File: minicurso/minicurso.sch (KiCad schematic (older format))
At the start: 4 parts

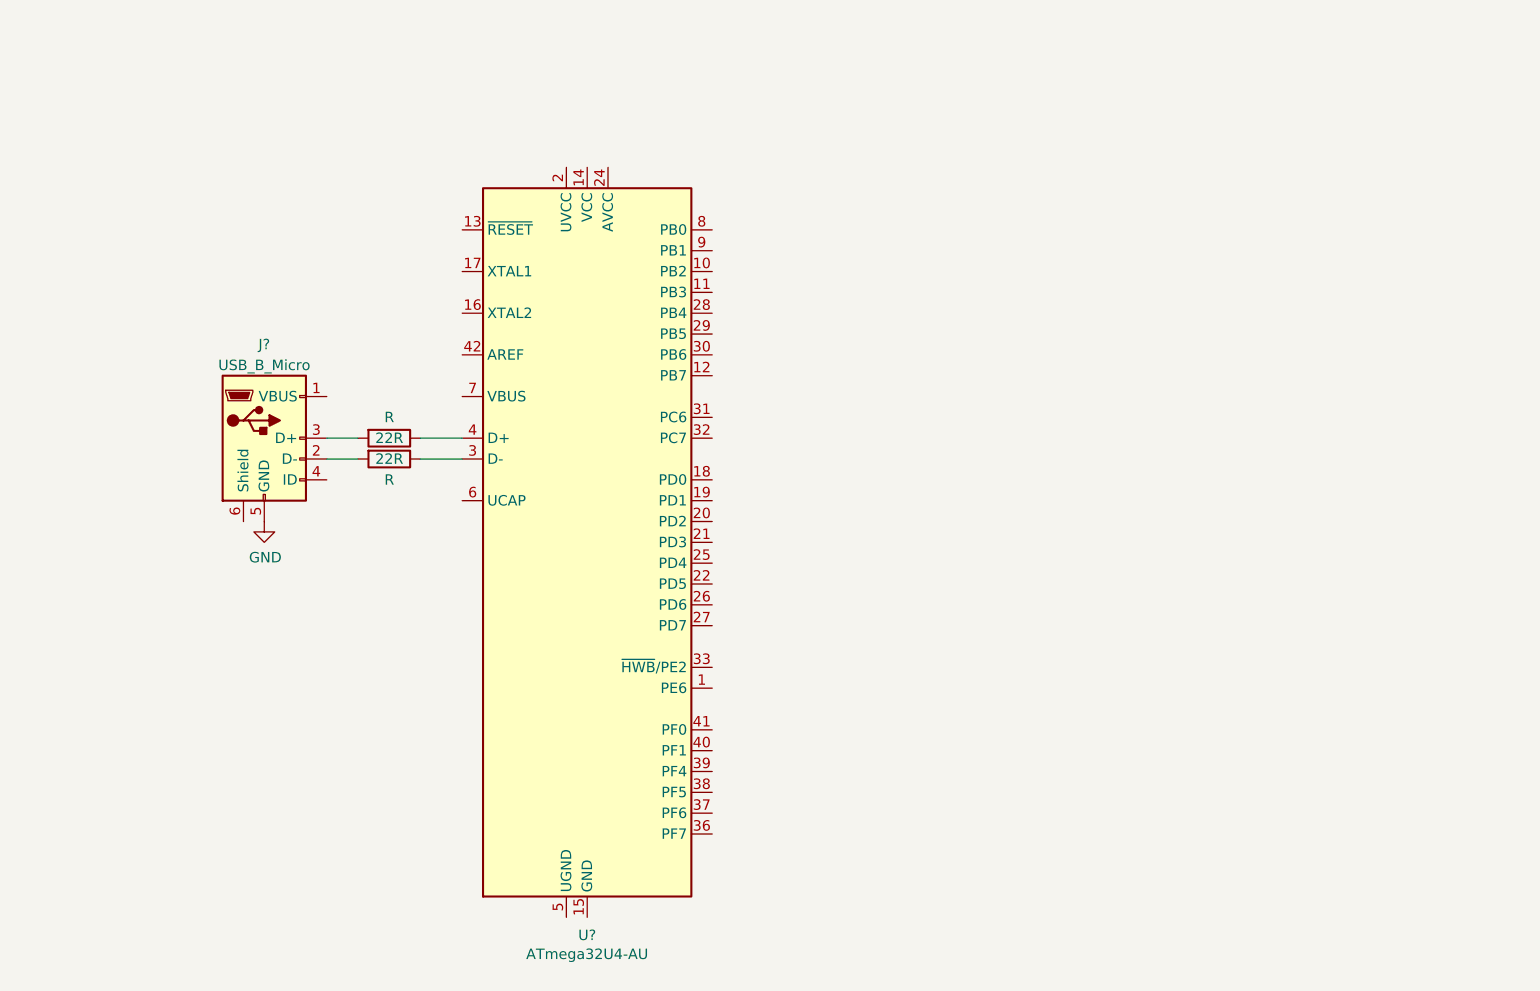
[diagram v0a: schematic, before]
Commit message: Add crystal, ucamp and bypass
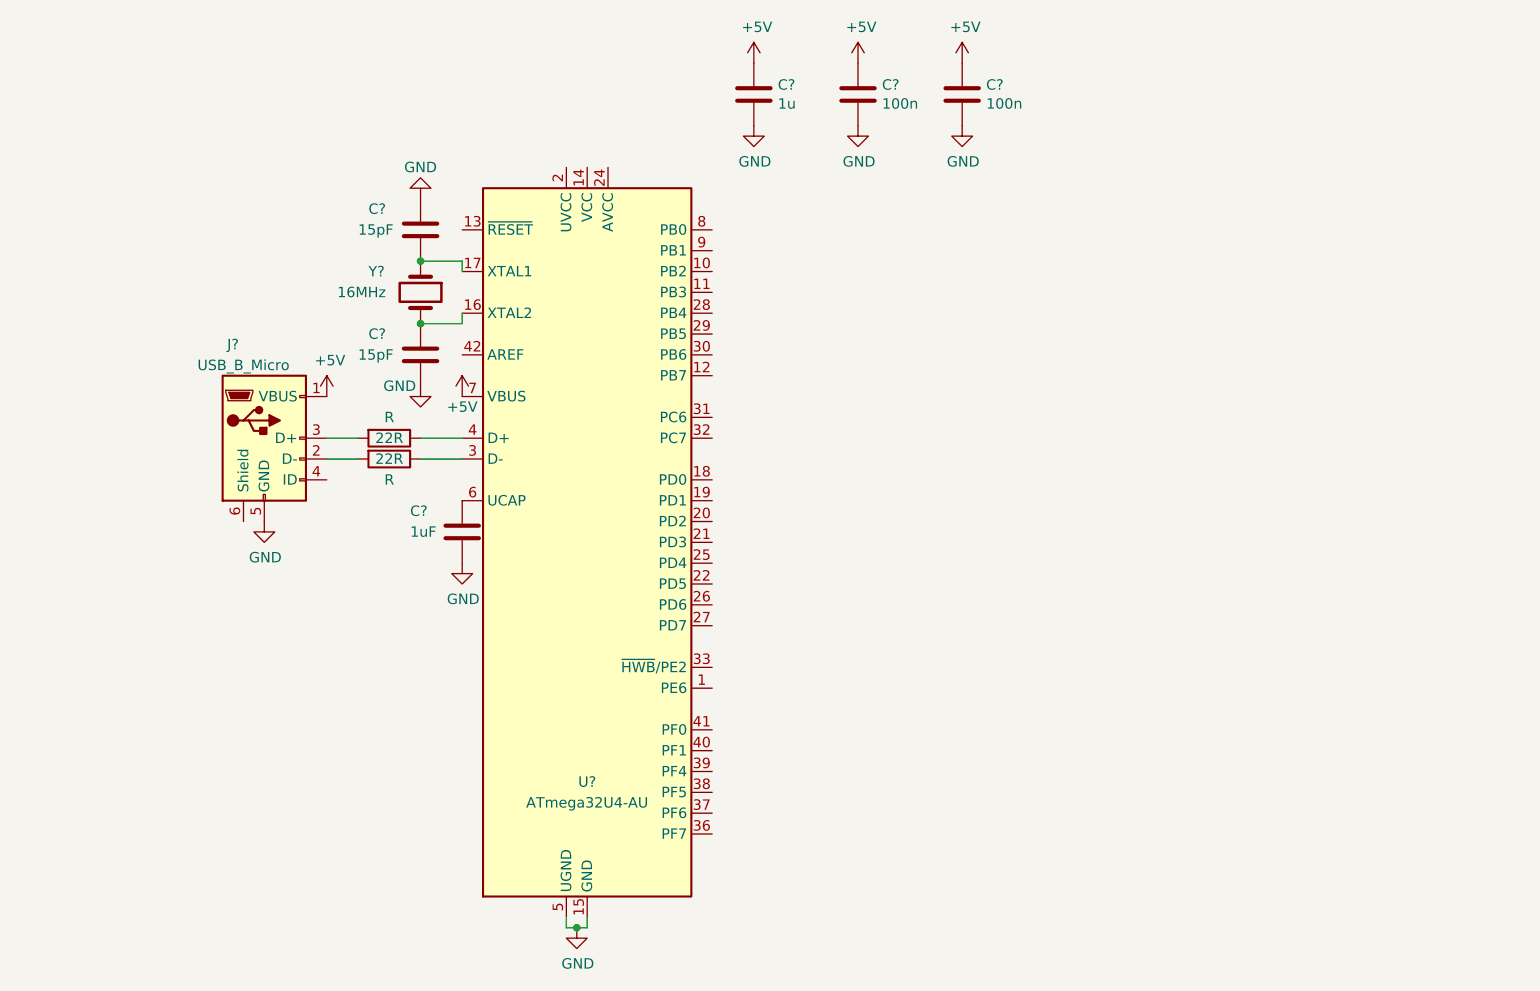
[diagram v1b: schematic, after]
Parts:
- added C? (x2): 15pF, symbol Device:C
- added C?: 1uF, symbol Device:C
- added C?: 1u, symbol Device:C
- added C? (x2): 100n, symbol Device:C
- added Y?: 16MHz, symbol Device:Crystal
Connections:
- net GND: now also U?.15 (GND), U?.23 (GND), U?.35 (GND), U?.43 (GND), U?.5 (UGND), C?.1, C?.2, C?.2, C?.2, C?.2, C?.2
- net at U?.16 (XTAL2): now also C?.1, Y?.2
- net at U?.17 (XTAL1): now also C?.2, Y?.1
- net at U?.6 (UCAP): now also C?.1
- net +5V: now reaches U?.7 (VBUS)
- net +5V: now also J?.1 (VBUS), C?.1, C?.1, C?.1
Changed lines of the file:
@@
 U 1 1 5D7A3DE3
 P 4000 3000
-F 0 "U?" H 4000 1114 50  0000 C CNN
-F 1 "ATmega32U4-AU" H 4000 1023 50  0000 C CNN
+F 0 "U?" H 4000 1850 50  0000 C CNN
+F 1 "ATmega32U4-AU" H 4000 1750 50  0000 C CNN
 F 2 "Package_QFP:TQFP-44_10x10mm_P0.8mm" H 4000 3000 50  0001 C CIN
 F 3 "http://ww1.microchip.com/downloads/en/DeviceDoc/Atmel-7766-8-bit-AVR-ATmega16U4-32U4_Datasheet.pdf" H 4000 3000 50  0001 C CNN
@@
 U 1 1 5D7A3F22
 P 2450 2500
-F 0 "J?" H 2450 2950 50  0000 C CNN
-F 1 "USB_B_Micro" H 2450 2850 50  0000 C CNN
+F 0 "J?" H 2300 2950 50  0000 C CNN
+F 1 "USB_B_Micro" H 2350 2850 50  0000 C CNN
 F 2 "" H 2600 2450 50  0001 C CNN
 F 3 "~" H 2600 2450 50  0001 C CNN
@@
 	1    0    0    -1
 $EndComp
+$Comp
+L power:GND #PWR?
+U 1 1 5D7A4F01
+P 3950 4850
+F 0 "#PWR?" H 3950 4600 50  0001 C CNN
+F 1 "GND" H 3955 4677 50  0000 C CNN
+F 2 "" H 3950 4850 50  0001 C CNN
+F 3 "" H 3950 4850 50  0001 C CNN
+	1    3950 4850
+	1    0    0    -1
+$EndComp
+Wire Wire Line
+	4000 4850 3950 4850
+Wire Wire Line
+	3900 4850 3900 4800
+Connection ~ 3950 4850
+Wire Wire Line
+	3950 4850 3900 4850
+Wire Wire Line
+	4000 4850 4000 4800
+$Comp
+L Device:Crystal Y?
+U 1 1 5D7A53EA
+P 3200 1800
+F 0 "Y?" V 3100 1550 50  0000 L CNN
+F 1 "16MHz" V 3200 1400 50  0000 L CNN
+F 2 "" H 3200 1800 50  0001 C CNN
+F 3 "~" H 3200 1800 50  0001 C CNN
+	1    3200 1800
+	0    1    1    0
+$EndComp
+Wire Wire Line
+	3400 1650 3400 1700
+Wire Wire Line
+	3400 1950 3400 1900
+Wire Wire Line
+	3200 1950 3400 1950
+Wire Wire Line
+	3200 1650 3400 1650
+$Comp
+L Device:C C?
+U 1 1 5D7A6541
+P 3200 1500
+F 0 "C?" H 2950 1600 50  0000 L CNN
+F 1 "15pF" H 2900 1500 50  0000 L CNN
+F 2 "" H 3238 1350 50  0001 C CNN
+F 3 "~" H 3200 1500 50  0001 C CNN
+	1    3200 1500
+	1    0    0    -1
+$EndComp
+Connection ~ 3200 1650
+$Comp
+L power:GND #PWR?
+U 1 1 5D7A65E6
+P 3200 1350
+F 0 "#PWR?" H 3200 1100 50  0001 C CNN
+F 1 "GND" H 3200 1200 50  0000 C CNN
+F 2 "" H 3200 1350 50  0001 C CNN
+F 3 "" H 3200 1350 50  0001 C CNN
+	1    3200 1350
+	-1   0    0    1
+$EndComp
+$Comp
+L Device:C C?
+U 1 1 5D7A66D4
+P 3200 2100
+F 0 "C?" H 2950 2200 50  0000 L CNN
+F 1 "15pF" H 2900 2100 50  0000 L CNN
+F 2 "" H 3238 1950 50  0001 C CNN
+F 3 "~" H 3200 2100 50  0001 C CNN
+	1    3200 2100
+	1    0    0    -1
+$EndComp
+Connection ~ 3200 1950
+$Comp
+L power:GND #PWR?
+U 1 1 5D7A6801
+P 3200 2250
+F 0 "#PWR?" H 3200 2000 50  0001 C CNN
+F 1 "GND" H 3100 2250 50  0000 C CNN
+F 2 "" H 3200 2250 50  0001 C CNN
+F 3 "" H 3200 2250 50  0001 C CNN
+	1    3200 2250
+	1    0    0    -1
+$EndComp
+$Comp
+L power:+5V #PWR?
+U 1 1 5D7A6D12
+P 2750 2300
+F 0 "#PWR?" H 2750 2150 50  0001 C CNN
+F 1 "+5V" H 2765 2473 50  0000 C CNN
+F 2 "" H 2750 2300 50  0001 C CNN
+F 3 "" H 2750 2300 50  0001 C CNN
+	1    2750 2300
+	1    0    0    -1
+$EndComp
+$Comp
+L power:+5V #PWR?
+U 1 1 5D7A6EC6
+P 3400 2300
+F 0 "#PWR?" H 3400 2150 50  0001 C CNN
+F 1 "+5V" H 3400 2250 50  0000 C CNN
+F 2 "" H 3400 2300 50  0001 C CNN
+F 3 "" H 3400 2300 50  0001 C CNN
+	1    3400 2300
+	1    0    0    -1
+$EndComp
+$Comp
+L Device:C C?
+U 1 1 5D7A6F9F
+P 3400 2950
+F 0 "C?" H 3150 3050 50  0000 L CNN
+F 1 "1uF" H 3150 2950 50  0000 L CNN
+F 2 "" H 3438 2800 50  0001 C CNN
+F 3 "~" H 3400 2950 50  0001 C CNN
+	1    3400 2950
+	1    0    0    -1
+$EndComp
+$Comp
+L power:GND #PWR?
+U 1 1 5D7A6FFB
+P 3400 3100
+F 0 "#PWR?" H 3400 2850 50  0001 C CNN
+F 1 "GND" H 3405 2927 50  0000 C CNN
+F 2 "" H 3400 3100 50  0001 C CNN
+F 3 "" H 3400 3100 50  0001 C CNN
+	1    3400 3100
+	1    0    0    -1
+$EndComp
+$Comp
+L power:+5V #PWR?
+U 1 1 5D7A4BAC
+P 4800 700
+F 0 "#PWR?" H 4800 550 50  0001 C CNN
+F 1 "+5V" H 4815 873 50  0000 C CNN
+F 2 "" H 4800 700 50  0001 C CNN
+F 3 "" H 4800 700 50  0001 C CNN
+	1    4800 700
+	1    0    0    -1
+$EndComp
+$Comp
+L Device:C C?
+U 1 1 5D7A7E2D
+P 4800 850
+F 0 "C?" H 4915 896 50  0000 L CNN
+F 1 "1u" H 4915 805 50  0000 L CNN
+F 2 "" H 4838 700 50  0001 C CNN
+F 3 "~" H 4800 850 50  0001 C CNN
+	1    4800 850
+	1    0    0    -1
+$EndComp
+$Comp
+L power:GND #PWR?
+U 1 1 5D7A7F18
+P 4800 1000
+F 0 "#PWR?" H 4800 750 50  0001 C CNN
+F 1 "GND" H 4805 827 50  0000 C CNN
+F 2 "" H 4800 1000 50  0001 C CNN
+F 3 "" H 4800 1000 50  0001 C CNN
+	1    4800 1000
+	1    0    0    -1
+$EndComp
+$Comp
+L Device:C C?
+U 1 1 5D7A81A9
+P 5300 850
+F 0 "C?" H 5415 896 50  0000 L CNN
+F 1 "100n" H 5415 805 50  0000 L CNN
+F 2 "" H 5338 700 50  0001 C CNN
+F 3 "~" H 5300 850 50  0001 C CNN
+	1    5300 850
+	1    0    0    -1
+$EndComp
+$Comp
+L power:+5V #PWR?
+U 1 1 5D7A8211
+P 5300 700
+F 0 "#PWR?" H 5300 550 50  0001 C CNN
+F 1 "+5V" H 5315 873 50  0000 C CNN
+F 2 "" H 5300 700 50  0001 C CNN
+F 3 "" H 5300 700 50  0001 C CNN
+	1    5300 700
+	1    0    0    -1
+$EndComp
+$Comp
+L power:GND #PWR?
+U 1 1 5D7A8230
+P 5300 1000
+F 0 "#PWR?" H 5300 750 50  0001 C CNN
+F 1 "GND" H 5305 827 50  0000 C CNN
+F 2 "" H 5300 1000 50  0001 C CNN
+F 3 "" H 5300 1000 50  0001 C CNN
+	1    5300 1000
+	1    0    0    -1
+$EndComp
+$Comp
+L Device:C C?
+U 1 1 5D7A841B
+P 5800 850
+F 0 "C?" H 5915 896 50  0000 L CNN
+F 1 "100n" H 5915 805 50  0000 L CNN
+F 2 "" H 5838 700 50  0001 C CNN
+F 3 "~" H 5800 850 50  0001 C CNN
+	1    5800 850
+	1    0    0    -1
+$EndComp
+$Comp
+L power:+5V #PWR?
+U 1 1 5D7A8457
+P 5800 700
+F 0 "#PWR?" H 5800 550 50  0001 C CNN
+F 1 "+5V" H 5815 873 50  0000 C CNN
+F 2 "" H 5800 700 50  0001 C CNN
+F 3 "" H 5800 700 50  0001 C CNN
+	1    5800 700
+	1    0    0    -1
+$EndComp
+$Comp
+L power:GND #PWR?
+U 1 1 5D7A8478
+P 5800 1000
+F 0 "#PWR?" H 5800 750 50  0001 C CNN
+F 1 "GND" H 5805 827 50  0000 C CNN
+F 2 "" H 5800 1000 50  0001 C CNN
+F 3 "" H 5800 1000 50  0001 C CNN
+	1    5800 1000
+	1    0    0    -1
+$EndComp

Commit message: Add reset and pinheaders
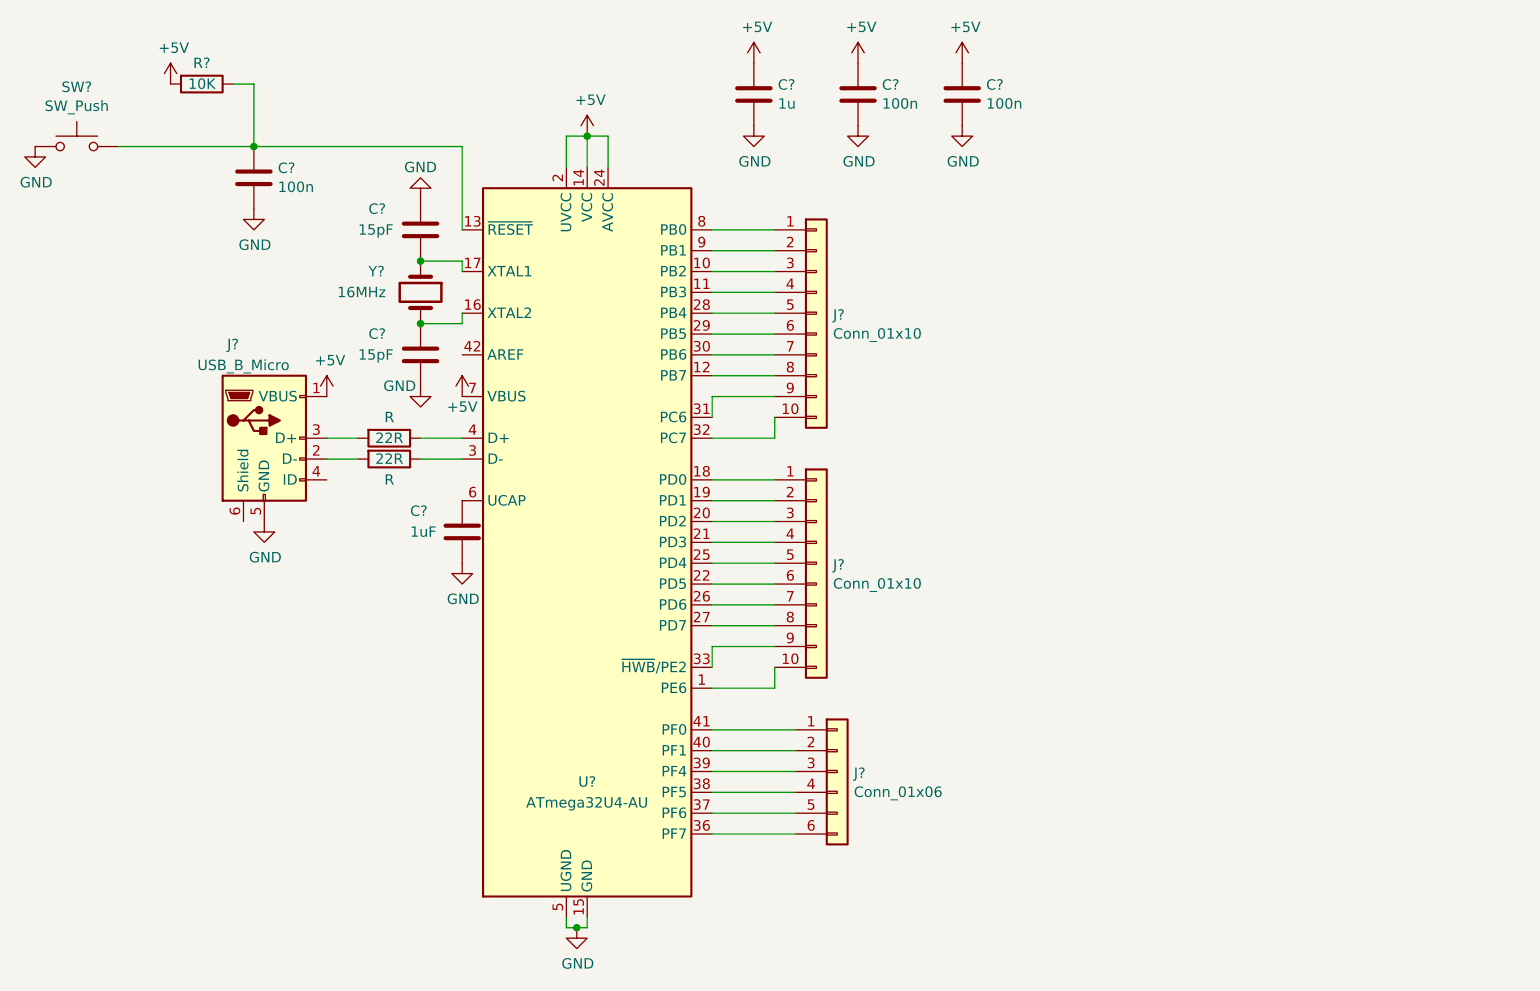
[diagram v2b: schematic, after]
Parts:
- added C?: 100n, symbol Device:C
- added J? (x2): Conn_01x10, symbol Connector_Generic:Conn_01x10
- added J?: Conn_01x06, symbol Connector_Generic:Conn_01x06
- added R?: 10K, symbol Device:R
- added SW?: SW_Push, symbol Switch:SW_Push
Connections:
- net +5V: now also U?.14 (VCC), U?.2 (UVCC), U?.24 (AVCC), U?.34 (VCC), U?.44 (AVCC), R?.2
- net GND: now also C?.2, SW?.1
- net at U?.1 (PE6): now also J?.10 (Pin_10)
- net at U?.10 (PB2): now also J?.3 (Pin_3)
- net at U?.11 (PB3): now also J?.4 (Pin_4)
- net at U?.12 (PB7): now also J?.8 (Pin_8)
- net at U?.13 (~RESET): now also C?.1, R?.1, SW?.2
- net at U?.18 (PD0): now also J?.1 (Pin_1)
- net at U?.19 (PD1): now also J?.2 (Pin_2)
- net at U?.20 (PD2): now also J?.3 (Pin_3)
- net at U?.21 (PD3): now also J?.4 (Pin_4)
- net at U?.22 (PD5): now also J?.6 (Pin_6)
- net at U?.25 (PD4): now also J?.5 (Pin_5)
- net at U?.26 (PD6): now also J?.7 (Pin_7)
- net at U?.27 (PD7): now also J?.8 (Pin_8)
- net at U?.28 (PB4): now also J?.5 (Pin_5)
- net at U?.29 (PB5): now also J?.6 (Pin_6)
- net at U?.30 (PB6): now also J?.7 (Pin_7)
- net at U?.31 (PC6): now also J?.9 (Pin_9)
- net at U?.32 (PC7): now also J?.10 (Pin_10)
- net at U?.33 (~HWB~/PE2): now also J?.9 (Pin_9)
- net at U?.36 (PF7): now also J?.6 (Pin_6)
- net at U?.37 (PF6): now also J?.5 (Pin_5)
- net at U?.38 (PF5): now also J?.4 (Pin_4)
- net at U?.39 (PF4): now also J?.3 (Pin_3)
- net at U?.40 (PF1): now also J?.2 (Pin_2)
- net at U?.41 (PF0): now also J?.1 (Pin_1)
- net at U?.8 (PB0): now also J?.1 (Pin_1)
- net at U?.9 (PB1): now also J?.2 (Pin_2)
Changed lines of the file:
@@
 	1    0    0    -1
 $EndComp
+$Comp
+L power:+5V #PWR?
+U 1 1 5D7A8686
+P 4000 1050
+F 0 "#PWR?" H 4000 900 50  0001 C CNN
+F 1 "+5V" H 4015 1223 50  0000 C CNN
+F 2 "" H 4000 1050 50  0001 C CNN
+F 3 "" H 4000 1050 50  0001 C CNN
+	1    4000 1050
+	1    0    0    -1
+$EndComp
+Wire Wire Line
+	3900 1200 3900 1050
+Wire Wire Line
+	3900 1050 4000 1050
+Wire Wire Line
+	4000 1200 4000 1050
+Connection ~ 4000 1050
+Wire Wire Line
+	4100 1200 4100 1050
+Wire Wire Line
+	4100 1050 4000 1050
+$Comp
+L Switch:SW_Push SW?
+U 1 1 5D7A8A82
+P 1550 1100
+F 0 "SW?" H 1550 1385 50  0000 C CNN
+F 1 "SW_Push" H 1550 1294 50  0000 C CNN
+F 2 "" H 1550 1300 50  0001 C CNN
+F 3 "" H 1550 1300 50  0001 C CNN
+	1    1550 1100
+	1    0    0    -1
+$EndComp
+$Comp
+L power:GND #PWR?
+U 1 1 5D7A8C8D
+P 1350 1100
+F 0 "#PWR?" H 1350 850 50  0001 C CNN
+F 1 "GND" H 1355 927 50  0000 C CNN
+F 2 "" H 1350 1100 50  0001 C CNN
+F 3 "" H 1350 1100 50  0001 C CNN
+	1    1350 1100
+	1    0    0    -1
+$EndComp
+$Comp
+L Device:R R?
+U 1 1 5D7A8D6B
+P 2150 800
+F 0 "R?" V 2050 800 50  0000 C CNN
+F 1 "10K" V 2150 800 50  0000 C CNN
+F 2 "" V 2080 800 50  0001 C CNN
+F 3 "~" H 2150 800 50  0001 C CNN
+	1    2150 800
+	0    1    1    0
+$EndComp
+$Comp
+L power:+5V #PWR?
+U 1 1 5D7A8DFE
+P 2000 800
+F 0 "#PWR?" H 2000 650 50  0001 C CNN
+F 1 "+5V" H 2015 973 50  0000 C CNN
+F 2 "" H 2000 800 50  0001 C CNN
+F 3 "" H 2000 800 50  0001 C CNN
+	1    2000 800
+	1    0    0    -1
+$EndComp
+Wire Wire Line
+	3400 1500 3400 1100
+Wire Wire Line
+	3400 1100 2400 1100
+Wire Wire Line
+	2300 800  2400 800
+Wire Wire Line
+	2400 800  2400 1100
+Connection ~ 2400 1100
+Wire Wire Line
+	2400 1100 1750 1100
+$Comp
+L power:GND #PWR?
+U 1 1 5D7AA47D
+P 2400 1400
+F 0 "#PWR?" H 2400 1150 50  0001 C CNN
+F 1 "GND" H 2405 1227 50  0000 C CNN
+F 2 "" H 2400 1400 50  0001 C CNN
+F 3 "" H 2400 1400 50  0001 C CNN
+	1    2400 1400
+	1    0    0    -1
+$EndComp
+$Comp
+L Device:C C?
+U 1 1 5D7AA571
+P 2400 1250
+F 0 "C?" H 2515 1296 50  0000 L CNN
+F 1 "100n" H 2515 1205 50  0000 L CNN
+F 2 "" H 2438 1100 50  0001 C CNN
+F 3 "~" H 2400 1250 50  0001 C CNN
+	1    2400 1250
+	1    0    0    -1
+$EndComp
+$Comp
+L Connector_Generic:Conn_01x10 J?
+U 1 1 5D7AB30B
+P 5100 1900
+F 0 "J?" H 5180 1892 50  0000 L CNN
+F 1 "Conn_01x10" H 5180 1801 50  0000 L CNN
+F 2 "" H 5100 1900 50  0001 C CNN
+F 3 "~" H 5100 1900 50  0001 C CNN
+	1    5100 1900
+	1    0    0    -1
+$EndComp
+$Comp
+L Connector_Generic:Conn_01x06 J?
+U 1 1 5D7AB549
+P 5200 4100
+F 0 "J?" H 5280 4092 50  0000 L CNN
+F 1 "Conn_01x06" H 5280 4001 50  0000 L CNN
+F 2 "" H 5200 4100 50  0001 C CNN
+F 3 "~" H 5200 4100 50  0001 C CNN
+	1    5200 4100
+	1    0    0    -1
+$EndComp
+$Comp
+L Connector_Generic:Conn_01x10 J?
+U 1 1 5D7AB63B
+P 5100 3100
+F 0 "J?" H 5180 3092 50  0000 L CNN
+F 1 "Conn_01x10" H 5180 3001 50  0000 L CNN
+F 2 "" H 5100 3100 50  0001 C CNN
+F 3 "~" H 5100 3100 50  0001 C CNN
+	1    5100 3100
+	1    0    0    -1
+$EndComp
+Wire Wire Line
+	4600 1500 4900 1500
+Wire Wire Line
+	4600 1600 4900 1600
+Wire Wire Line
+	4600 1700 4900 1700
+Wire Wire Line
+	4600 1800 4900 1800
+Wire Wire Line
+	4600 1900 4900 1900
+Wire Wire Line
+	4600 2000 4900 2000
+Wire Wire Line
+	4600 2100 4900 2100
+Wire Wire Line
+	4900 2200 4600 2200
+Wire Wire Line
+	4600 2400 4600 2300
+Wire Wire Line
+	4600 2300 4900 2300
+Wire Wire Line
+	4600 2500 4900 2500
+Wire Wire Line
+	4900 2500 4900 2400
+Wire Wire Line
+	4600 2700 4900 2700
+Wire Wire Line
+	4600 2800 4900 2800
+Wire Wire Line
+	4600 2900 4900 2900
+Wire Wire Line
+	4600 3000 4900 3000
+Wire Wire Line
+	4600 3100 4900 3100
+Wire Wire Line
+	4600 3200 4900 3200
+Wire Wire Line
+	4600 3300 4900 3300
+Wire Wire Line
+	4600 3400 4900 3400
+Wire Wire Line
+	4600 3600 4600 3500
+Wire Wire Line
+	4600 3500 4900 3500
+Wire Wire Line
+	4600 3700 4900 3700
+Wire Wire Line
+	4900 3700 4900 3600
+Wire Wire Line
+	4600 3900 5000 3900
+Wire Wire Line
+	4600 4000 5000 4000
+Wire Wire Line
+	5000 4100 4600 4100
+Wire Wire Line
+	4600 4200 5000 4200
+Wire Wire Line
+	5000 4300 4600 4300
+Wire Wire Line
+	4600 4400 5000 4400
 $EndSCHEMATC
